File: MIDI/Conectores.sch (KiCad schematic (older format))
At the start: 4 parts, among them J4 CONN_01X06, J5 CONN_01X06

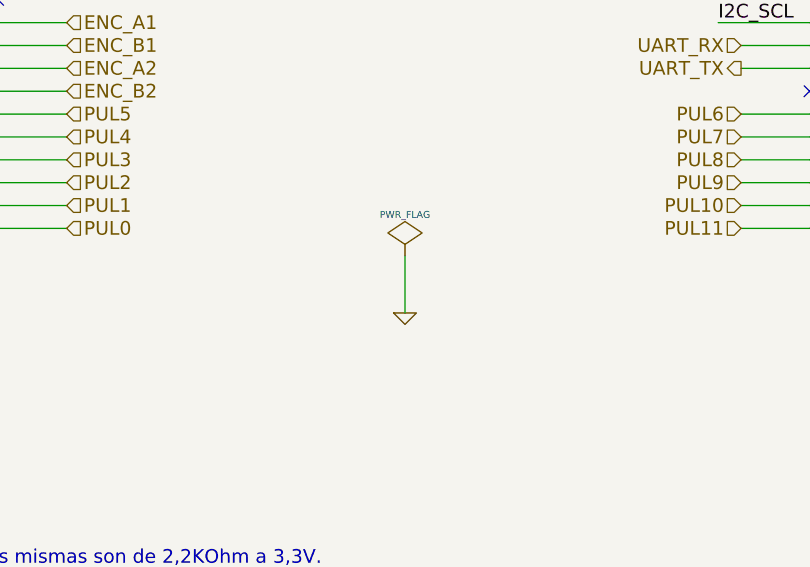
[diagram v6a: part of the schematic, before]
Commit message: Se incluye Power Flag y correción final
> Se incluye Power Flag para el símbolo GNDA
> Se incluye correción final por parte de Mg. Ing. Diego Javier Brengi
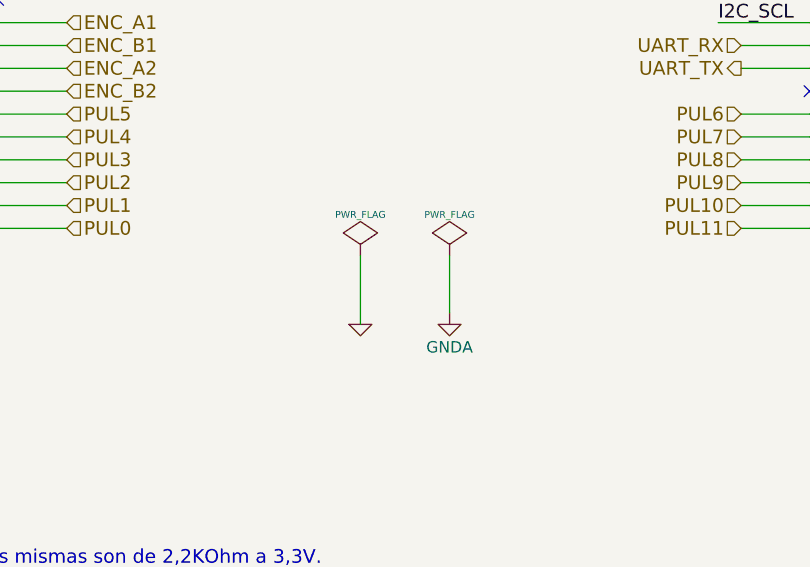
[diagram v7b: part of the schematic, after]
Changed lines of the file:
@@
 L PWR_FLAG #FLG026
 U 1 1 5947169C
-P 5825 5450
-F 0 "#FLG026" H 5825 5545 30  0001 C CNN
-F 1 "PWR_FLAG" H 5825 5630 30  0000 C CNN
-F 2 "" H 5825 5450 60  0000 C CNN
-F 3 "" H 5825 5450 60  0000 C CNN
-	1    5825 5450
+P 5630 5450
+F 0 "#FLG026" H 5630 5545 30  0001 C CNN
+F 1 "PWR_FLAG" H 5630 5630 30  0000 C CNN
+F 2 "" H 5630 5450 60  0000 C CNN
+F 3 "" H 5630 5450 60  0000 C CNN
+	1    5630 5450
 	1    0    0    -1
 $EndComp
@@
 L GND #PWR027
 U 1 1 594716FF
-P 5825 5700
-F 0 "#PWR027" H 5825 5700 30  0001 C CNN
-F 1 "GND" H 5825 5630 30  0001 C CNN
-F 2 "" H 5825 5700 60  0000 C CNN
-F 3 "" H 5825 5700 60  0000 C CNN
-	1    5825 5700
+P 5630 5750
+F 0 "#PWR027" H 5630 5750 30  0001 C CNN
+F 1 "GND" H 5630 5680 30  0001 C CNN
+F 2 "" H 5630 5750 60  0000 C CNN
+F 3 "" H 5630 5750 60  0000 C CNN
+	1    5630 5750
 	1    0    0    -1
 $EndComp
@@
 Notas:
 $Comp
-L GNDA #PWR?
+L GNDA #PWR028
 U 1 1 5990E91B
 P 9195 4230
-F 0 "#PWR?" H 9195 3980 50  0001 C CNN
+F 0 "#PWR028" H 9195 3980 50  0001 C CNN
 F 1 "GNDA" H 9195 4080 50  0000 C CNN
 F 2 "" H 9195 4230 50  0001 C CNN
@@
 	8895 3430 8895 3330
 Wire Wire Line
-	5825 5450 5825 5700
+	5630 5450 5630 5750
 Connection ~ 8895 5330
 Connection ~ 8895 5230
@@
 	7195 2380 7195 4130
 $Comp
-L GNDA #PWR?
+L GNDA #PWR029
 U 1 1 5990EC64
 P 7395 2130
-F 0 "#PWR?" H 7395 1880 50  0001 C CNN
+F 0 "#PWR029" H 7395 1880 50  0001 C CNN
 F 1 "GNDA" H 7395 1980 50  0000 C CNN
 F 2 "" H 7395 2130 50  0001 C CNN
@@
 Wire Wire Line
 	7145 2180 6795 2180
+$Comp
+L GNDA #PWR030
+U 1 1 599C3ADB
+P 6020 5700
+F 0 "#PWR030" H 6020 5450 50  0001 C CNN
+F 1 "GNDA" H 6020 5550 50  0000 C CNN
+F 2 "" H 6020 5700 50  0001 C CNN
+F 3 "" H 6020 5700 50  0001 C CNN
+	1    6020 5700
+	1    0    0    -1
+$EndComp
+$Comp
+L PWR_FLAG #FLG031
+U 1 1 599C3B9B
+P 6020 5450
+F 0 "#FLG031" H 6020 5545 30  0001 C CNN
+F 1 "PWR_FLAG" H 6020 5630 30  0000 C CNN
+F 2 "" H 6020 5450 60  0000 C CNN
+F 3 "" H 6020 5450 60  0000 C CNN
+	1    6020 5450
+	1    0    0    -1
+$EndComp
+Wire Wire Line
+	6020 5450 6020 5700
 $EndSCHEMATC
